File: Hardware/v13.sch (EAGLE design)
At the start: 86 parts, among them J1 22-27-2081-08, J2 22-27-2031-03

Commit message: added 5v pin header for twi added optional pull-ups for twi moved some parts around and rerouted some wires
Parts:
- added R36, R37: 4k7, rcl:R-EU_R0603
- I2C: value 22-27-2031-03 -> 22-27-2041-04; device con-molex:22-27-2031-03 -> con-molex:22-27-2041-04
- R25: value 6.2k -> 6k2
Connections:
- net GND: now also I2C-4.S; no longer I2C-3.S
- net SCL: now also I2C-3.S, R37.1; no longer I2C-2.S
- net SDA: now also I2C-2.S, R36.1; no longer I2C-1.S
- net VCC: now also I2C-1.S, R36.2, R37.2
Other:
- note added: "(optional) Pull-Ups"
- moved on the sheet: I2C-1, I2C-2, I2C-3
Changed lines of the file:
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@@
 <?xml version="1.0" encoding="utf-8"?>
 <!DOCTYPE eagle SYSTEM "eagle.dtd">
-<eagle version="6.5.0">
+<eagle version="7.2.0">
 <drawing>
 <settings>
@@
 <part name="R24" library="rcl" deviceset="R-EU_" device="R0603" value="100k"/>
 <part name="R27" library="rcl" deviceset="R-EU_" device="R0603" value="11k"/>
-<part name="R25" library="rcl" deviceset="R-EU_" device="R0603" value="6.2k"/>
+<part name="R25" library="rcl" deviceset="R-EU_" device="R0603" value="6k2"/>
 <part name="GND23" library="supply1" deviceset="GND" device=""/>
 <part name="P+12" library="supply1" deviceset="VCC" device=""/>
 <part name="GND24" library="supply1" deviceset="GND" device=""/>
 <part name="GND25" library="supply1" deviceset="GND" device=""/>
-<part name="I2C" library="con-molex" deviceset="22-?-03" device="27-2031"/>
 <part name="GND3" library="supply1" deviceset="GND" device=""/>
 <part name="GND26" library="supply1" deviceset="GND" device=""/>
@@
 <part name="GND34" library="supply1" deviceset="GND" device=""/>
 <part name="SAFETY" library="pinhead" deviceset="PINHD-1X2" device=""/>
+<part name="R36" library="rcl" deviceset="R-EU_" device="R0603" value="4k7"/>
+<part name="R37" library="rcl" deviceset="R-EU_" device="R0603" value="4k7"/>
+<part name="P+2" library="supply1" deviceset="VCC" device=""/>
+<part name="I2C" library="con-molex" deviceset="22-?-04" device="27-2041"/>
+<part name="P+8" library="supply1" deviceset="VCC" device=""/>
 </parts>
 <sheets>
@@
 <text x="609.6" y="53.34" size="3.81" layer="97">Pin Header</text>
 <text x="114.3" y="66.04" size="3.81" layer="97">LM324 for the safety circuit</text>
+<wire x1="1003.3" y1="86.36" x2="1066.8" y2="86.36" width="0.1524" layer="97"/>
+<wire x1="1003.3" y1="43.18" x2="1003.3" y2="86.36" width="0.1524" layer="97"/>
+<wire x1="1066.8" y1="86.36" x2="1066.8" y2="43.18" width="0.1524" layer="97"/>
+<wire x1="1066.8" y1="43.18" x2="1003.3" y2="43.18" width="0.1524" layer="97"/>
+<text x="1005.84" y="45.72" size="3.81" layer="97">(optional) Pull-Ups</text>
 </plain>
 <instances>
@@
 <instance part="GND24" gate="1" x="523.24" y="20.32"/>
 <instance part="GND25" gate="1" x="480.06" y="20.32"/>
-<instance part="I2C" gate="-1" x="678.18" y="129.54"/>
-<instance part="I2C" gate="-2" x="678.18" y="124.46"/>
-<instance part="I2C" gate="-3" x="678.18" y="119.38"/>
 <instance part="GND3" gate="1" x="673.1" y="116.84"/>
 <instance part="GND26" gate="1" x="50.8" y="88.9"/>
@@
 <instance part="GND34" gate="1" x="38.1" y="88.9"/>
 <instance part="SAFETY" gate="G$1" x="314.96" y="121.92" rot="R90"/>
+<instance part="R36" gate="G$1" x="1033.78" y="76.2" rot="R180"/>
+<instance part="R37" gate="G$1" x="1033.78" y="66.04" rot="R180"/>
+<instance part="P+2" gate="VCC" x="1016" y="81.28"/>
+<instance part="I2C" gate="-1" x="678.18" y="134.62"/>
+<instance part="I2C" gate="-2" x="678.18" y="129.54"/>
+<instance part="I2C" gate="-3" x="678.18" y="124.46"/>
+<instance part="I2C" gate="-4" x="678.18" y="119.38"/>
+<instance part="P+8" gate="VCC" x="673.1" y="137.16"/>
 </instances>
 <busses>
@@
 <junction x="129.54" y="121.92"/>
 <wire x1="129.54" y1="121.92" x2="129.54" y2="124.46" width="0.1524" layer="91"/>
+</segment>
+<segment>
+<pinref part="P+2" gate="VCC" pin="VCC"/>
+<wire x1="1016" y1="78.74" x2="1016" y2="76.2" width="0.1524" layer="91"/>
+<pinref part="R36" gate="G$1" pin="2"/>
+<wire x1="1016" y1="76.2" x2="1028.7" y2="76.2" width="0.1524" layer="91"/>
+<pinref part="R37" gate="G$1" pin="2"/>
+<wire x1="1028.7" y1="66.04" x2="1016" y2="66.04" width="0.1524" layer="91"/>
+<wire x1="1016" y1="66.04" x2="1016" y2="76.2" width="0.1524" layer="91"/>
+<junction x="1016" y="76.2"/>
+</segment>
+<segment>
+<pinref part="P+8" gate="VCC" pin="VCC"/>
+<pinref part="I2C" gate="-1" pin="S"/>
+<wire x1="673.1" y1="134.62" x2="675.64" y2="134.62" width="0.1524" layer="91"/>
 </segment>
 </net>
@@
 </segment>
 <segment>
-<pinref part="I2C" gate="-3" pin="S"/>
 <pinref part="GND3" gate="1" pin="GND"/>
 <wire x1="675.64" y1="119.38" x2="673.1" y2="119.38" width="0.1524" layer="91"/>
+<pinref part="I2C" gate="-4" pin="S"/>
 </segment>
 <segment>
@@
 </segment>
 <segment>
-<pinref part="I2C" gate="-1" pin="S"/>
 <wire x1="670.56" y1="129.54" x2="675.64" y2="129.54" width="0.1524" layer="91"/>
 <label x="670.56" y="129.54" size="1.778" layer="95" rot="R180" xref="yes"/>
+<pinref part="I2C" gate="-2" pin="S"/>
+</segment>
+<segment>
+<pinref part="R36" gate="G$1" pin="1"/>
+<wire x1="1043.94" y1="76.2" x2="1038.86" y2="76.2" width="0.1524" layer="91"/>
+<label x="1043.94" y="76.2" size="1.778" layer="95" xref="yes"/>
 </segment>
 </net>
@@
 </segment>
 <segment>
-<pinref part="I2C" gate="-2" pin="S"/>
 <wire x1="670.56" y1="124.46" x2="675.64" y2="124.46" width="0.1524" layer="91"/>
 <label x="670.56" y="124.46" size="1.778" layer="95" rot="R180" xref="yes"/>
-</segment>
-</net>
+<pinref part="I2C" gate="-3" pin="S"/>
+</segment>
+<segment>
+<pinref part="R37" gate="G$1" pin="1"/>
+<wire x1="1043.94" y1="66.04" x2="1038.86" y2="66.04" width="0.1524" layer="91"/>
+<label x="1043.94" y="66.04" size="1.778" layer="95" xref="yes"/>
+</segment>
+</net>

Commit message: [hardware] Adds A4 frame to schematic, Signalnames
and changed name of signal of pwm output to PWM_OUT
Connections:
- net N$33 renamed PWM_OUT
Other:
- moved on the sheet: AVR, C1, C10, C11, C12, C13, C14, C15, C16, C17, C2, C3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

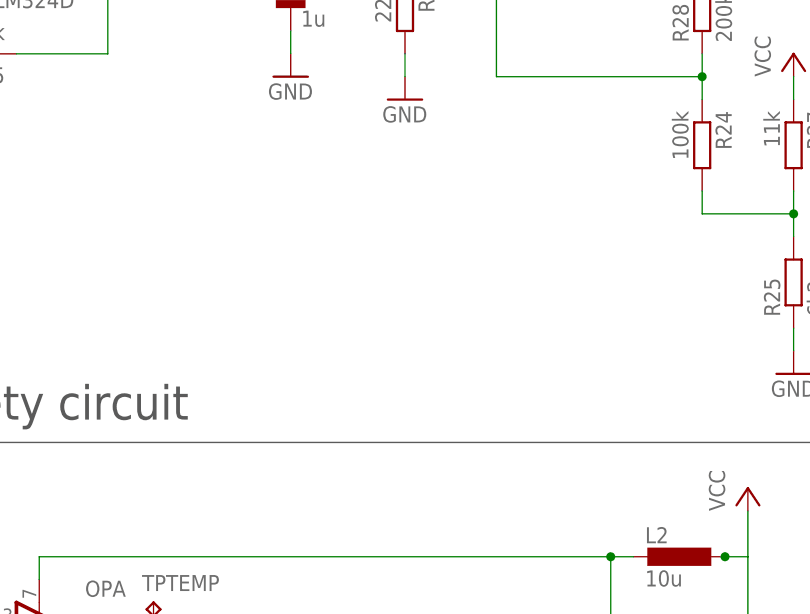
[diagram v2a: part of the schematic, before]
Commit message: changed radius of round corners changed location of the drilling holes slightly cleared some space around the drilling holes added 2x 10k to set all unused LM324 inputs to a 2,5V moved some components around
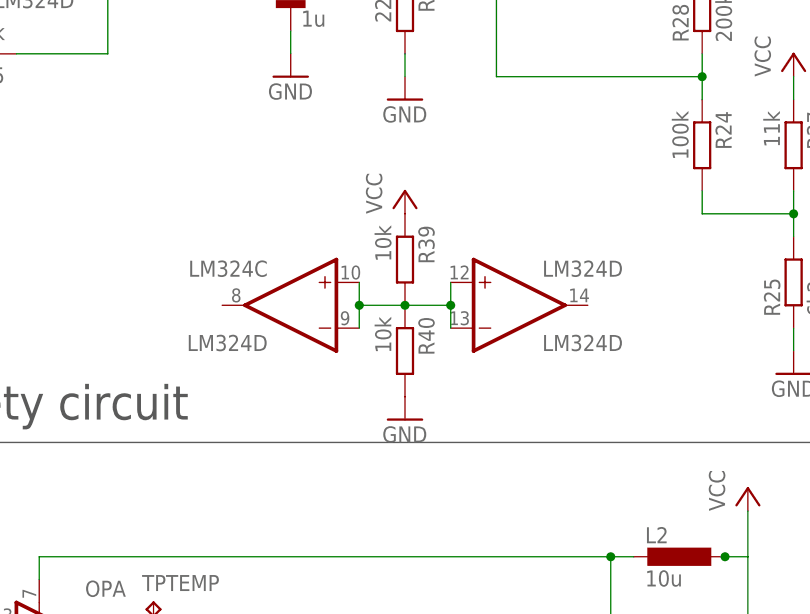
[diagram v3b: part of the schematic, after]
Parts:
- added R39, R40: 10k, rcl:R-EU_R0603
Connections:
- new net N$4: LM324C.+IN, LM324C.-IN, LM324D.+IN, LM324D.-IN, R39.2, R40.1
- net GND: now also R40.2
- net VCC: now also R39.1
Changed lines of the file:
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@@
 <?xml version="1.0" encoding="utf-8"?>
 <!DOCTYPE eagle SYSTEM "eagle.dtd">
-<eagle version="7.3.0">
+<eagle version="7.2.0">
 <drawing>
 <settings>
@@
 <part name="P+8" library="supply1" deviceset="VCC" device=""/>
 <part name="FRAME2" library="frames" deviceset="A3L-LOC" device=""/>
+<part name="R39" library="rcl" deviceset="R-EU_" device="R0603" value="10k"/>
+<part name="R40" library="rcl" deviceset="R-EU_" device="R0603" value="10k"/>
+<part name="P+14" library="supply1" deviceset="VCC" device=""/>
+<part name="GND35" library="supply1" deviceset="GND" device=""/>
 </parts>
 <sheets>
@@
 <instance part="P+8" gate="VCC" x="287.02" y="251.46"/>
 <instance part="FRAME2" gate="G$1" x="0" y="0"/>
+<instance part="LM324" gate="C" x="86.36" y="116.84" rot="MR0"/>
+<instance part="LM324" gate="D" x="111.76" y="116.84"/>
+<instance part="R39" gate="G$1" x="99.06" y="121.92" rot="R270"/>
+<instance part="R40" gate="G$1" x="99.06" y="111.76" rot="R270"/>
+<instance part="P+14" gate="VCC" x="99.06" y="129.54"/>
+<instance part="GND35" gate="1" x="99.06" y="104.14"/>
 </instances>
 <busses>
@@
 <pinref part="I2C" gate="-1" pin="S"/>
 <wire x1="287.02" y1="248.92" x2="289.56" y2="248.92" width="0.1524" layer="91"/>
+</segment>
+<segment>
+<pinref part="R39" gate="G$1" pin="1"/>
+<pinref part="P+14" gate="VCC" pin="VCC"/>
 </segment>
 </net>
@@
 <wire x1="152.4" y1="132.08" x2="152.4" y2="134.62" width="0.1524" layer="91"/>
 </segment>
+<segment>
+<pinref part="R40" gate="G$1" pin="2"/>
+<pinref part="GND35" gate="1" pin="GND"/>
+</segment>
 </net>
 <net name="N$1" class="0">
@@
 </segment>
 </net>
+<net name="N$4" class="0">
+<segment>
+<pinref part="LM324" gate="C" pin="+IN"/>
+<pinref part="LM324" gate="C" pin="-IN"/>
+<wire x1="93.98" y1="119.38" x2="93.98" y2="116.84" width="0.1524" layer="91"/>
+<pinref part="R40" gate="G$1" pin="1"/>
+<pinref part="R39" gate="G$1" pin="2"/>
+<wire x1="93.98" y1="116.84" x2="93.98" y2="114.3" width="0.1524" layer="91"/>
+<wire x1="93.98" y1="116.84" x2="99.06" y2="116.84" width="0.1524" layer="91"/>
+<junction x="93.98" y="116.84"/>
+<junction x="99.06" y="116.84"/>
+<pinref part="LM324" gate="D" pin="+IN"/>
+<wire x1="99.06" y1="116.84" x2="104.14" y2="116.84" width="0.1524" layer="91"/>
+<wire x1="104.14" y1="116.84" x2="104.14" y2="119.38" width="0.1524" layer="91"/>
+<pinref part="LM324" gate="D" pin="-IN"/>
+<wire x1="104.14" y1="116.84" x2="104.14" y2="114.3" width="0.1524" layer="91"/>
+<junction x="104.14" y="116.84"/>
+</segment>
+</net>

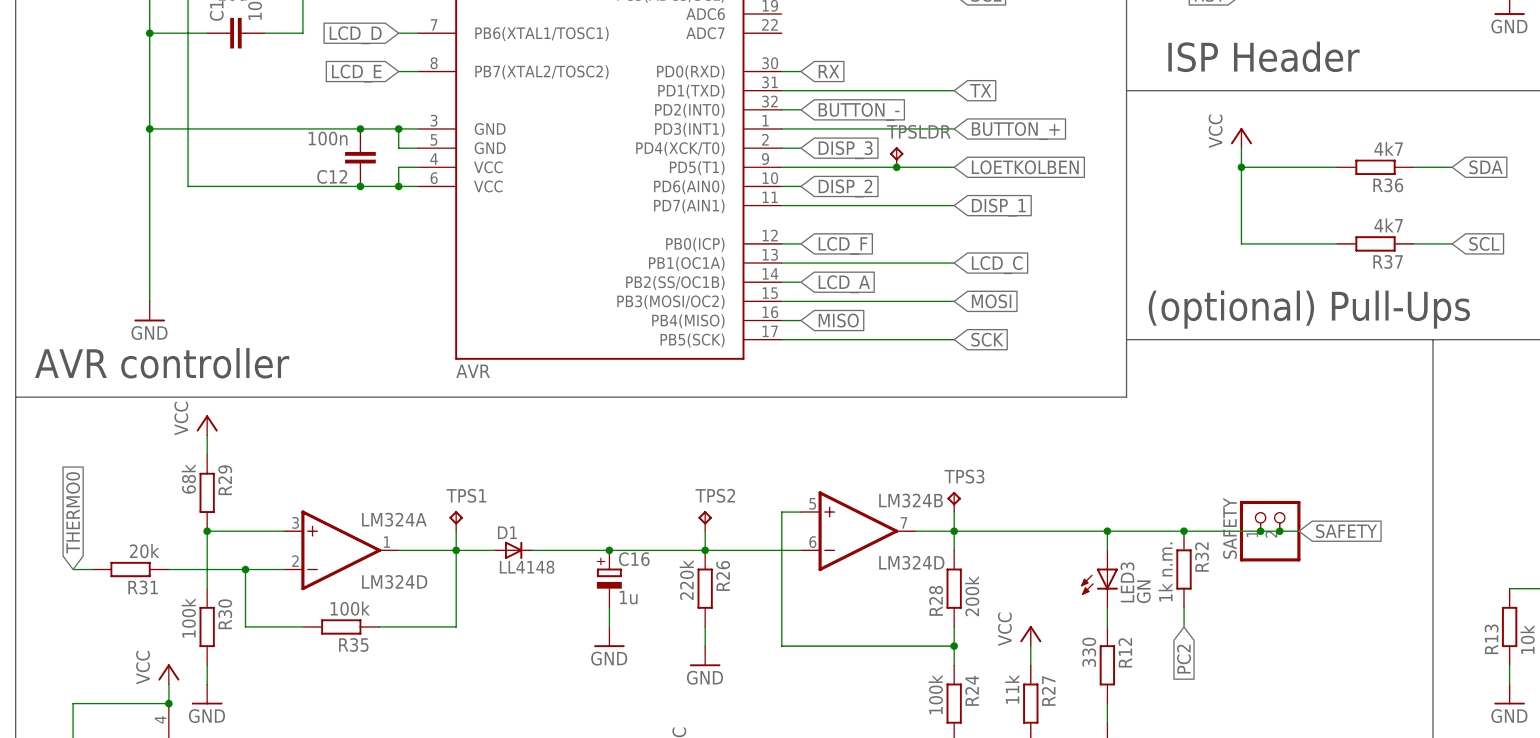
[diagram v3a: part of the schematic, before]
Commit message: change some resistor values moved the leds to lower left corner
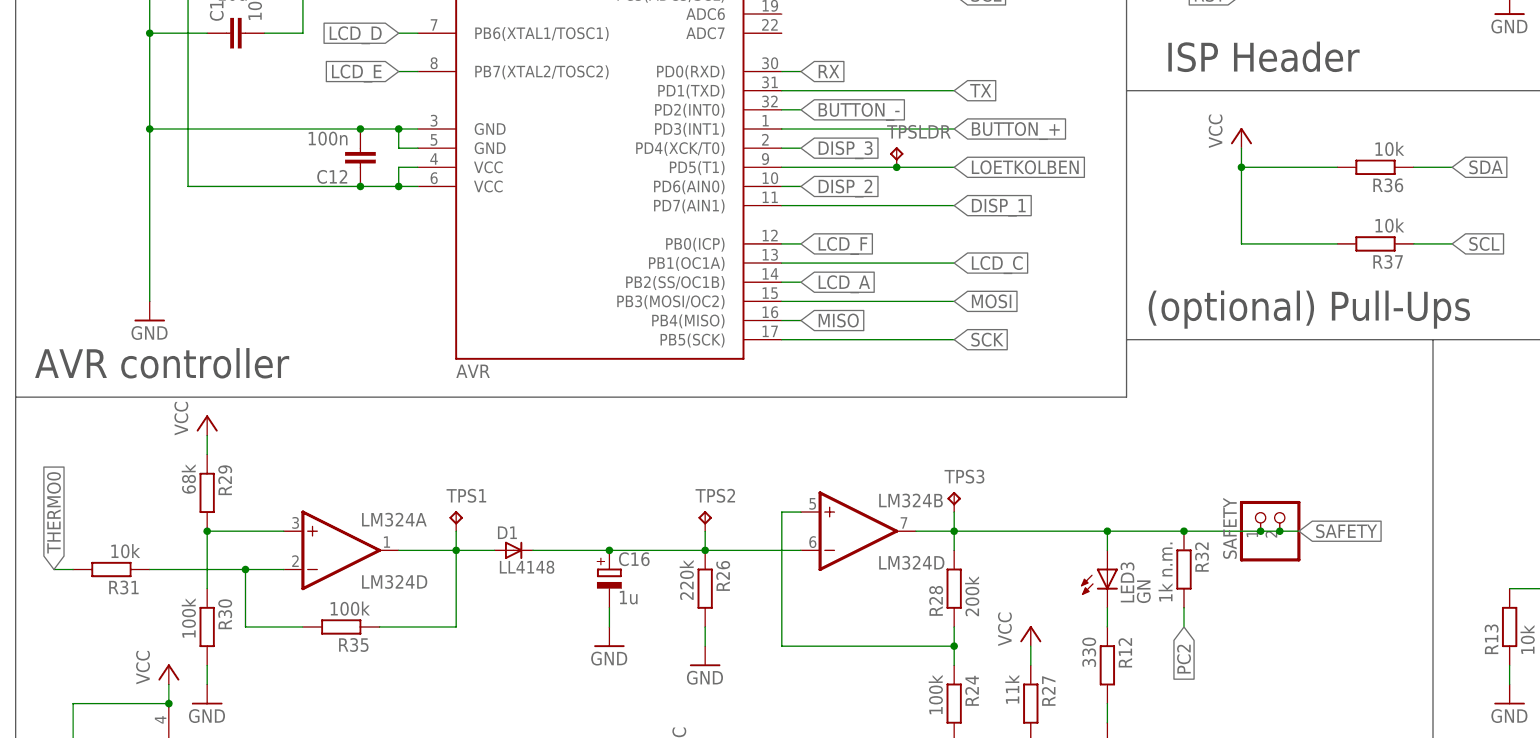
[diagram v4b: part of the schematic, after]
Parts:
- R31: value 20k -> 10k
- R36, R37: value 4k7 -> 10k
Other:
- moved on the sheet: R31
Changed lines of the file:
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@@
 <part name="R35" library="rcl" deviceset="R-EU_" device="R0603" value="100k"/>
 <part name="R30" library="rcl" deviceset="R-EU_" device="R0603" value="100k"/>
-<part name="R31" library="rcl" deviceset="R-EU_" device="R0603" value="20k"/>
+<part name="R31" library="rcl" deviceset="R-EU_" device="R0603" value="10k"/>
 <part name="R29" library="rcl" deviceset="R-EU_" device="R0603" value="68k"/>
 <part name="GND16" library="supply1" deviceset="GND" device=""/>
@@
 <part name="GND34" library="supply1" deviceset="GND" device=""/>
 <part name="SAFETY" library="pinhead" deviceset="PINHD-1X2" device=""/>
-<part name="R36" library="rcl" deviceset="R-EU_" device="R0603" value="4k7"/>
-<part name="R37" library="rcl" deviceset="R-EU_" device="R0603" value="4k7"/>
+<part name="R36" library="rcl" deviceset="R-EU_" device="R0603" value="10k"/>
+<part name="R37" library="rcl" deviceset="R-EU_" device="R0603" value="10k"/>
 <part name="P+2" library="supply1" deviceset="VCC" device=""/>
 <part name="I2C" library="con-molex" deviceset="22-?-04" device="27-2041"/>
@@
 <instance part="R35" gate="G$1" x="50.8" y="144.78" rot="R180"/>
 <instance part="R30" gate="G$1" x="33.02" y="144.78" rot="R270"/>
-<instance part="R31" gate="G$1" x="22.86" y="152.4" rot="R180"/>
+<instance part="R31" gate="G$1" x="20.32" y="152.4" rot="R180"/>
 <instance part="R29" gate="G$1" x="33.02" y="162.56" rot="R270"/>
 <instance part="GND16" gate="1" x="33.02" y="134.62"/>
@@
 <segment>
 <pinref part="R31" gate="G$1" pin="2"/>
-<wire x1="17.78" y1="152.4" x2="15.24" y2="152.4" width="0.1524" layer="91"/>
-<label x="15.24" y="152.4" size="1.778" layer="95" rot="R90" xref="yes"/>
+<wire x1="15.24" y1="152.4" x2="12.7" y2="152.4" width="0.1524" layer="91"/>
+<label x="12.7" y="152.4" size="1.778" layer="95" rot="R90" xref="yes"/>
 </segment>
 </net>
@@
 </segment>
 </net>
-<net name="N$6" class="0">
-<segment>
-<pinref part="R31" gate="G$1" pin="1"/>
-<pinref part="LM324" gate="A" pin="-IN"/>
-<wire x1="27.94" y1="152.4" x2="38.1" y2="152.4" width="0.1524" layer="91"/>
-<wire x1="38.1" y1="152.4" x2="43.18" y2="152.4" width="0.1524" layer="91"/>
-<wire x1="38.1" y1="152.4" x2="38.1" y2="144.78" width="0.1524" layer="91"/>
-<junction x="38.1" y="152.4"/>
-<pinref part="R35" gate="G$1" pin="2"/>
-<wire x1="38.1" y1="144.78" x2="45.72" y2="144.78" width="0.1524" layer="91"/>
-</segment>
-</net>
 <net name="N$7" class="0">
 <segment>
@@
 </segment>
 </net>
+<net name="N$3" class="0">
+<segment>
+<pinref part="R31" gate="G$1" pin="1"/>
+<pinref part="LM324" gate="A" pin="-IN"/>
+<wire x1="38.1" y1="152.4" x2="43.18" y2="152.4" width="0.1524" layer="91"/>
+<wire x1="38.1" y1="152.4" x2="38.1" y2="144.78" width="0.1524" layer="91"/>
+<pinref part="R35" gate="G$1" pin="2"/>
+<wire x1="38.1" y1="144.78" x2="45.72" y2="144.78" width="0.1524" layer="91"/>
+<wire x1="25.4" y1="152.4" x2="38.1" y2="152.4" width="0.1524" layer="91"/>
+<junction x="38.1" y="152.4"/>
+</segment>
+</net>
